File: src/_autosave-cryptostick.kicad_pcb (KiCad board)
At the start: 2 copper layers, 21.8 x 16.3 mm, 33 parts, among them J1 SIM_JACKET, J2 USB_A, P1 CONN_4, U1 STM32F103TB, U2 CAT6217-330, U3 DF5A5.6JE, X1 12MHz, p1 debug-pin, p2 debug-pin, p3 debug-pin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

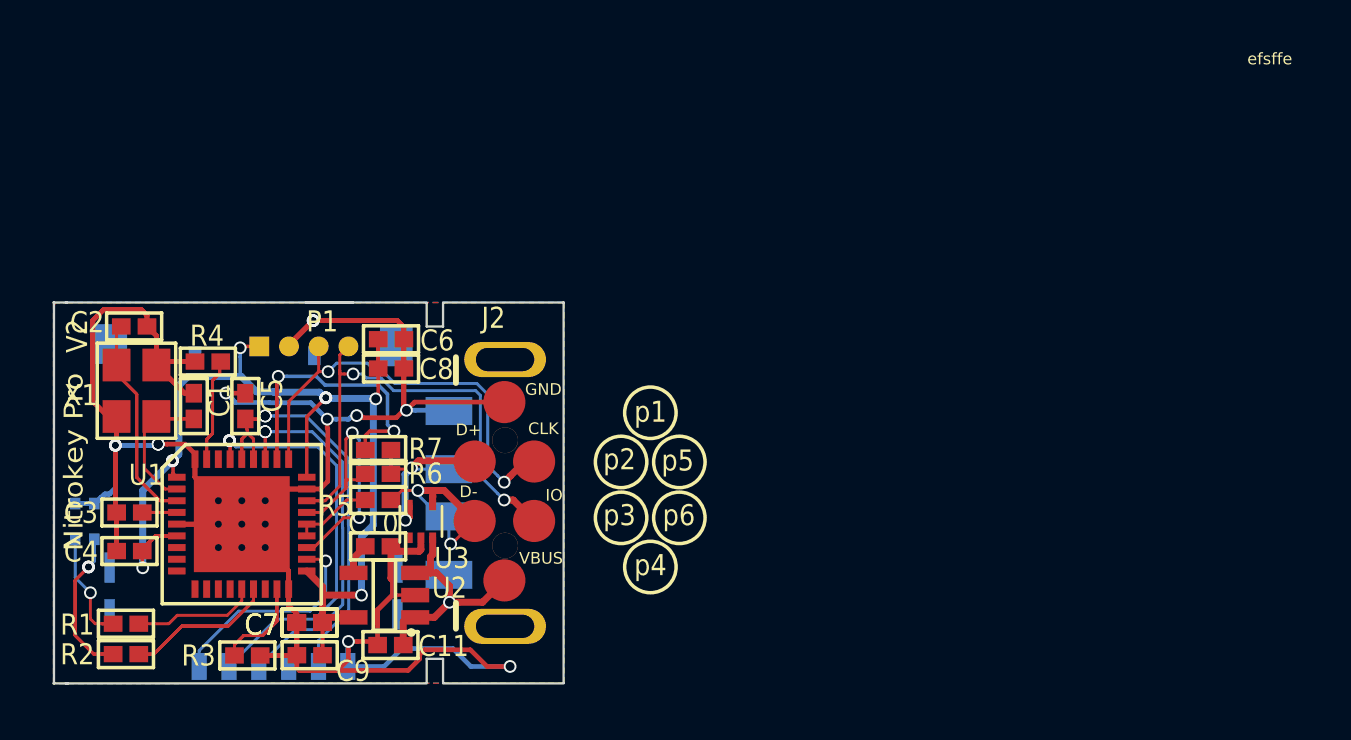
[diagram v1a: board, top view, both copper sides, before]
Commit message: V3: - ATECC508 crypto engine - Touch button, SIM jacket used as a touch pad, MTCH101 touch controller (same as used with Nitrokey U2F FIDO stick)
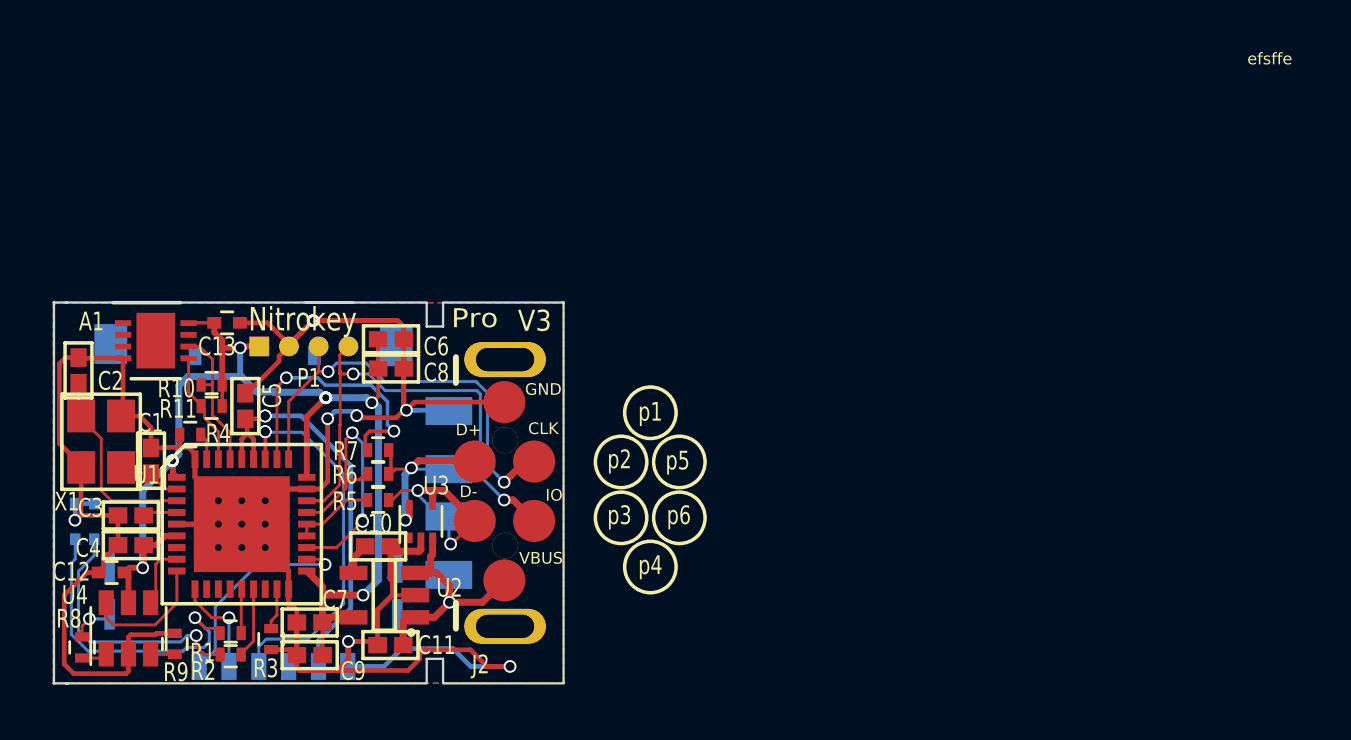
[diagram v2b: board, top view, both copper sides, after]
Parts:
- removed the C7 at (125.7, 104.5)
- added A1: ATECC508A, Housings_DFN_QFN:DFN-8-1EP_3x3mm_Pitch0.5mm, F.Cu at (119.1, 92.5)
- added C12: 0.1uF, C_0402, F.Cu at (117.2, 102.4)
- added C13: 0.1uF, Capacitors_SMD:C_0402, F.Cu at (122.1, 91.7)
- added R10: 10k, Resistors_SMD:R_0402, F.Cu at (121.5, 94.4)
- added R11: 10k, Resistors_SMD:R_0402, F.Cu at (121.5, 95.3)
- added R8: 4.7k, Resistors_SMD:R_0402, F.Cu at (115.9, 105.6)
- added R9: 10k, Resistors_SMD:R_0402, F.Cu at (119.9, 105.5)
- added U4: MTCH101, TO_SOT_Packages_SMD:SOT-23-6, F.Cu at (117.9, 104.8)
- R1, R2, R3, R4, R5, R6, R7: footprint r_0402 -> Resistors_SMD:R_0402
- moved R1 4.49 mm to (122.3, 105.0), turned to 0 degrees
- moved R2 4.48 mm to (122.3, 105.9), turned to 0 degrees
- moved R4 3.21 mm to (120.5, 96.5), turned to 180 degrees
- moved C2 3.03 mm to (115.8, 93.8), turned to 270 degrees
- moved C1 2.97 mm to (118.9, 97.6)
- moved X1 2.65 mm to (116.7, 96.8)
- moved R3 1.23 mm to (124.0, 105.3), turned to 90 degrees
- moved C4 0.26 mm to (118.0, 101.2), turned to 0 degrees
- moved C3 0.14 mm to (118.0, 100.0)
- turned R5 to 0 degrees
- turned R6 to 0 degrees
- turned R7 to 0 degrees
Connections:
- C4 pad 1: GND -> +3.3V
- C4 pad 2: +3.3V -> GND
- U1 pad 10: (no net) -> /SCSDA
- U1 pad 33: /SCSDA -> /I2C1_SCL
- U1 pad 34: (no net) -> /I2C1_SDA
- U1 pad 8: (no net) -> /BUTTON
- U1 pad 9: (no net) -> /BUTTON_RST
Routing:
- net GND: track 160.2 -> 138.8 mm, vias 12 -> 8
- net /SCSDA: track 18.1 -> 4.47 mm, vias 2 -> 1
- net Net-(R2-Pad2): track 12.7 -> 3.01 mm
- net /OSC_OUT: track 18.0 -> 8.40 mm
- net /BOOT0: track 8.84 -> 1.15 mm
- net Net-(D1-Pad1): track 6.56 -> 13.1 mm
- net /BOOT1: track 8.12 -> 1.79 mm
- net /I2C1_SCL: track 0.00 -> 6.31 mm
- net +3.3V: track 51.7 -> 57.9 mm
- net /BUTTON_RST: track 0.00 -> 5.55 mm
- net /OSC_IN: track 8.07 -> 2.80 mm
- net /I2C1_SDA: track 0.00 -> 4.84 mm
- net /USB_EN: track 15.4 -> 11.7 mm
- net Net-(R1-Pad2): track 5.31 -> 1.89 mm
- net Net-(D1-Pad4): track 14.1 -> 11.2 mm, vias 2 -> 1
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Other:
- net class VDD: trace_width 0.1524 -> 0.25
- board text added: "Nitrokey"
- board text added: "Pro"
- board text added: "V3"
- board text removed: "V2"
